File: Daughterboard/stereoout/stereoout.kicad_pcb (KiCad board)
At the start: 2 copper layers, 203.4 x 174 mm, 22 parts, among them J1 Conn_01x33, J10 AudioJack2, J11 AudioJack2, J12 AudioJack3, J13 Conn_01x09, J2 Conn_01x04, J3 Conn_01x09, J4 Conn_01x37, J5 Conn_01x37, J6 AudioJack2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

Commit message: Finalize design and add Gerbers for first PCB run
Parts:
- added G***: LOGO, stereoout:stereo_outs_panel_holes, F.Cu at (65.0, 104.0)
- added G***: LOGO, stereoout:stereo_outs_panel_holes, F.Cu at (200.0, 103.0)
- moved J11 7.34 mm to (197.0, 178.0)
- moved J12 3.86 mm to (232.0, 178.0)
- moved J10 3.65 mm to (165.0, 178.0)
- moved J13 1.98 mm to (191.8, 156.3)
- moved J8 1.52 mm to (165.0, 86.0)
- moved J9 1.52 mm to (165.0, 116.0)
- moved J6 1.52 mm to (165.0, 26.0)
- moved J7 1.52 mm to (165.0, 56.0)
- moved J3 0.73 mm to (56.8, 157.3)
- moved RV2 0.73 mm to (62.0, 57.0)
- moved RV3 0.73 mm to (62.0, 87.0)
- moved RV4 0.73 mm to (62.0, 117.0)
- moved RV6 0.73 mm to (97.0, 57.0)
- moved RV7 0.73 mm to (97.0, 87.0)
- moved RV8 0.73 mm to (97.0, 117.0)
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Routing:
- net Net-(J10-PadT): track 42.3 -> 46.3 mm
- net Net-(J12-PadR): track 37.1 -> 40.9 mm
- net Net-(J12-PadT): track 26.2 -> 28.3 mm
- net Net-(J13-Pad5): track 76.9 -> 78.9 mm
- net Net-(J13-Pad2): track 157.1 -> 159.1 mm
- net Net-(J13-Pad4): track 103.7 -> 105.7 mm
- net Net-(J13-Pad3): track 130.4 -> 132.4 mm
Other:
- board size 203.4 x 174 mm -> 203 x 174 mm
- board text added: "Stereo Out jacks board Rich Holmes Sep 2020"
- board text added: "Stereo Out pots board Rich Holmes Sep 2020"
- board text removed: "Stereo Out jacks board Rich Holmes 9/2020"
- board text removed: "Stereo Out pots board Rich Holmes 9/2020"

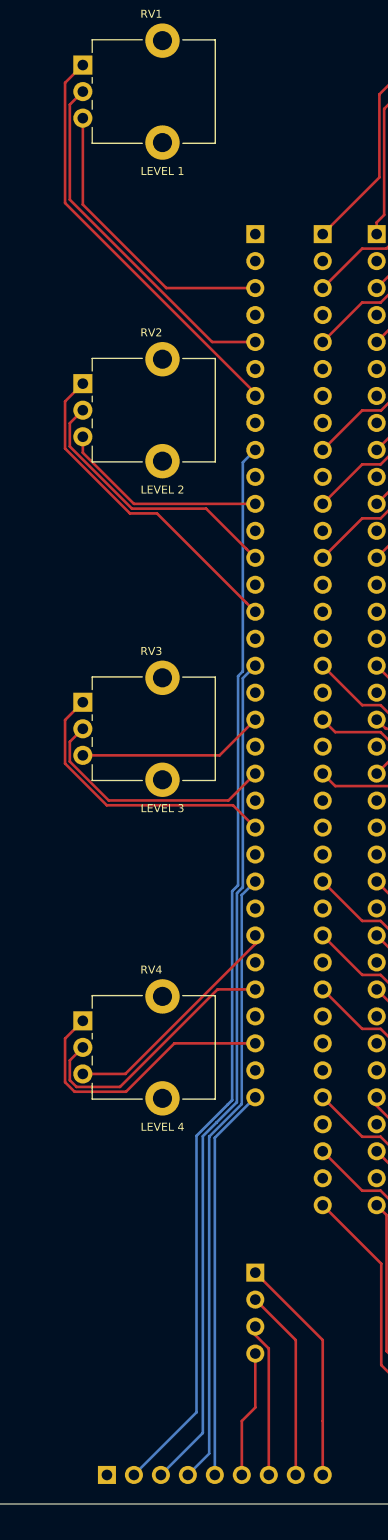
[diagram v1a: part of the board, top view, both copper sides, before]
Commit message: Fix wrong pot orientations and touch up routing
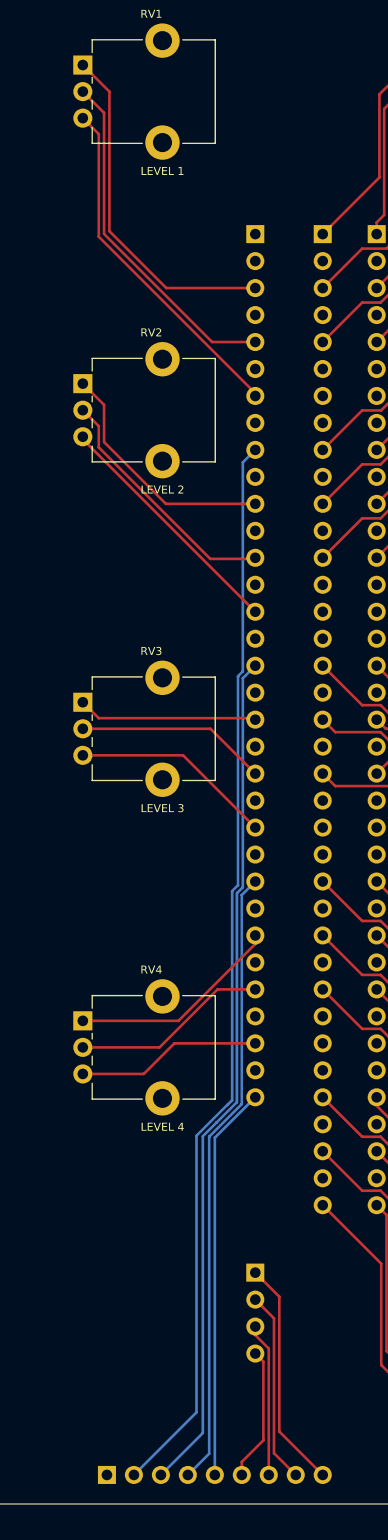
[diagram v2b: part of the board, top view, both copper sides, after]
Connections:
- J5 pad 23: /PAN4_4 -> Net-(J5-Pad23)
- J5 pad 25: /PAN4_5 -> /PAN4_4
- J5 pad 27: /PAN4_6 -> /PAN4_5
- J5 pad 29: Net-(J5-Pad29) -> /PAN4_6
- RV1 pad 1: /LEV1_3 -> /LEV1_1
- RV1 pad 3: /LEV1_1 -> /LEV1_3
- RV2 pad 1: /LEV2_3 -> /LEV2_1
- RV2 pad 3: /LEV2_1 -> /LEV2_3
- RV3 pad 1: /LEV3_3 -> /LEV3_1
- RV3 pad 3: /LEV3_1 -> /LEV3_3
- RV4 pad 1: /LEV4_3 -> /LEV4_1
- RV4 pad 3: /LEV4_1 -> /LEV4_3
- RV8 pad 4: /PAN4_5 -> /PAN4_4
- RV8 pad 5: /PAN4_6 -> /PAN4_5
- RV8 pad 6: Net-(J5-Pad29) -> /PAN4_6
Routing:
- net /PAN4_4: track 0.00 -> 15.1 mm
- net Net-(J5-Pad29): track 9.96 -> 0.00 mm
- net /LEV4_3: track 26.6 -> 17.4 mm
- net /LEV2_3: track 31.1 -> 23.2 mm
- net /LEV3_3: track 26.9 -> 19.1 mm
- net /LEV4_2: track 25.1 -> 18.5 mm
- net /LEV1_3: track 39.3 -> 32.9 mm
- net /LEV3_2: track 23.6 -> 18.0 mm
- net /LEV1_1: track 27.6 -> 32.6 mm
- net /LEV2_1: track 19.7 -> 23.0 mm
- net /PAN4_6: track 12.5 -> 9.96 mm
- net /PAN4_5: track 15.1 -> 12.5 mm
- net /LEV2_2: track 25.7 -> 23.3 mm
- net /LEV4_1: track 22.1 -> 20.0 mm
- net /LEV1_2: track 33.7 -> 32.7 mm
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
